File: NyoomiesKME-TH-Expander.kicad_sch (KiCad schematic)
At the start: 13 parts, among them J1 2x4 Dupont Socket, J2 JST XH 2 Pin, J3 JST XH 2 Pin, J4 JST XH 2 Pin, J5 JST XH 2 Pin

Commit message: fix capacitor part no.
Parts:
- C1, C2, C3, C4: LCSC Part # C29266 -> C47971
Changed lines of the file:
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@@
 			)
 		)
-		(property "LCSC Part #" "C29266"
+		(property "LCSC Part #" "C47971"
 			(at 125.73 88.9 0)
 			(effects
@@
 			)
 		)
-		(property "LCSC Part #" "C29266"
+		(property "LCSC Part #" "C47971"
 			(at 125.73 72.39 0)
 			(effects
@@
 			)
 		)
-		(property "LCSC Part #" "C29266"
+		(property "LCSC Part #" "C47971"
 			(at 125.73 121.92 0)
 			(effects
@@
 			)
 		)
-		(property "LCSC Part #" "C29266"
+		(property "LCSC Part #" "C47971"
 			(at 125.73 105.41 0)
 			(effects

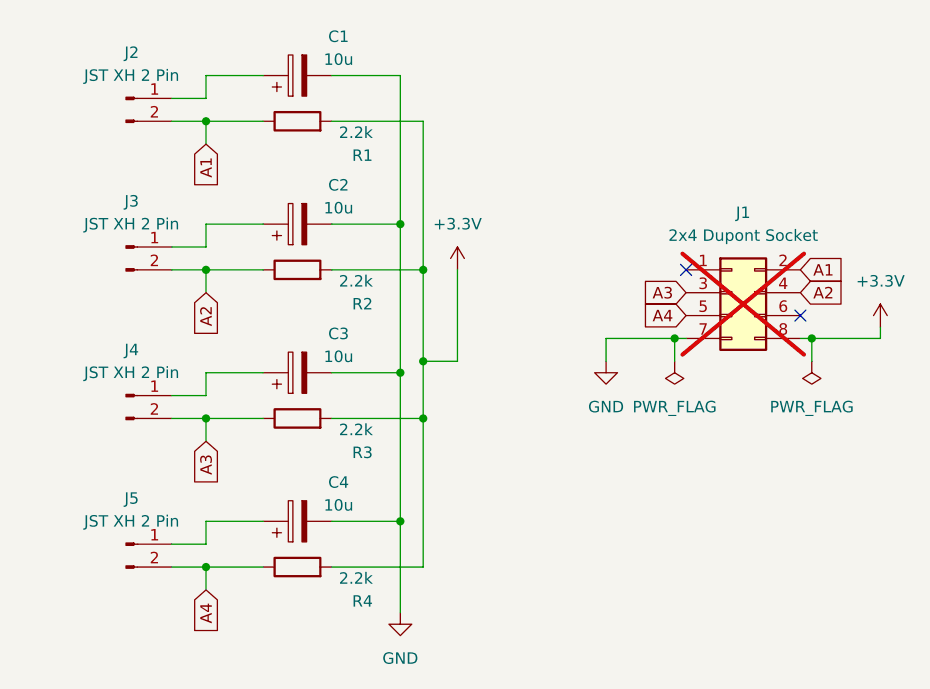
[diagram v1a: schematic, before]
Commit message: use filtering caps correctly and use labels instead of global labels
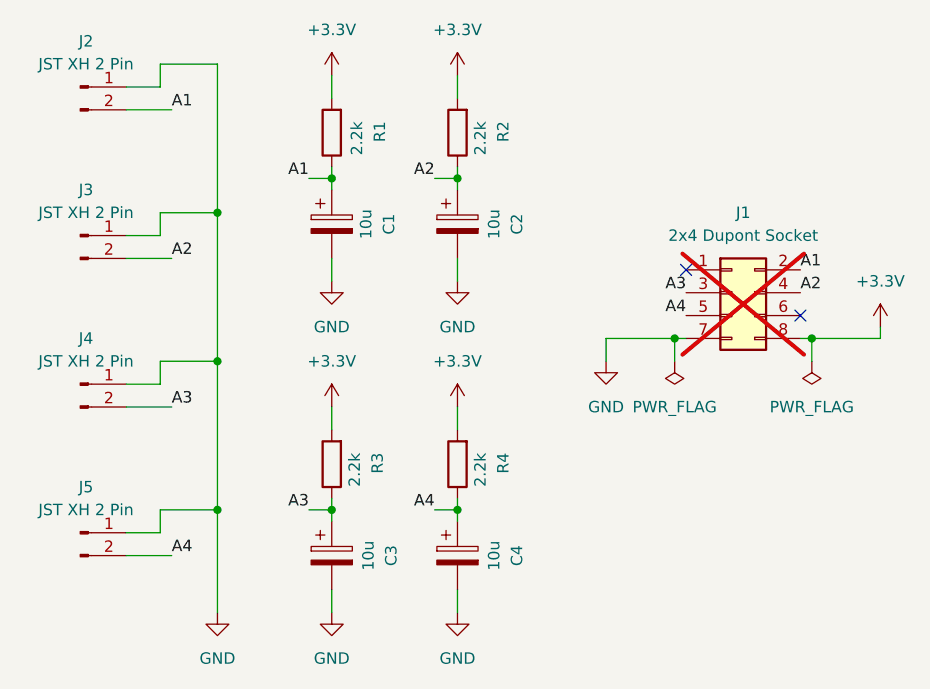
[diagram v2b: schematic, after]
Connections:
- net A1: now also C1.1
- net A2: now also C2.1
- net A3: now also C3.1
- net A4: now also C4.1
- net GND: now also J2.1 (Pin_1), J3.1 (Pin_1), J4.1 (Pin_1), J5.1 (Pin_1)
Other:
- moved on the sheet: C1, C2, C3, C4, J2, J3, J4, J5, R1, R2, R3, R4

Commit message: switch to unpolarized caps
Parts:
- C1, C2, C3, C4: symbol Device:C_Polarized -> Device:C
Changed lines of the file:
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@@
 	)
 	(symbol
-		(lib_id "Device:C_Polarized")
+		(lib_id "Device:C")
 		(at 143.51 88.9 0)
 		(unit 1)
@@
 			)
 		)
-		(property "Description" "Polarized capacitor"
+		(property "Description" "Unpolarized capacitor"
 			(at 143.51 88.9 0)
 			(effects
@@
 	)
 	(symbol
-		(lib_id "Device:C_Polarized")
+		(lib_id "Device:C")
 		(at 129.54 88.9 0)
 		(unit 1)
@@
 			)
 		)
-		(property "Description" "Polarized capacitor"
+		(property "Description" "Unpolarized capacitor"
 			(at 129.54 88.9 0)
 			(effects
@@
 	)
 	(symbol
-		(lib_id "Device:C_Polarized")
+		(lib_id "Device:C")
 		(at 143.51 125.73 0)
 		(unit 1)
@@
 			)
 		)
-		(property "Description" "Polarized capacitor"
+		(property "Description" "Unpolarized capacitor"
 			(at 143.51 125.73 0)
 			(effects
@@
 	)
 	(symbol
-		(lib_id "Device:C_Polarized")
+		(lib_id "Device:C")
 		(at 129.54 125.73 0)
 		(unit 1)
@@
 			)
 		)
-		(property "Description" "Polarized capacitor"
+		(property "Description" "Unpolarized capacitor"
 			(at 129.54 125.73 0)
 			(effects
